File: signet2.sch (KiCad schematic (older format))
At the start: 54 parts, among them IC1 THGBMHG8C2LBAIL, J1 480372200, J3 Conn_01x02_Male, SW1 EVQ_PLDA15, U1 LDFM33PUR, U2 STM32F733IEKx, U3 USBULC6-2M6, Y1 ABM10-167-12.000MHZ-T3

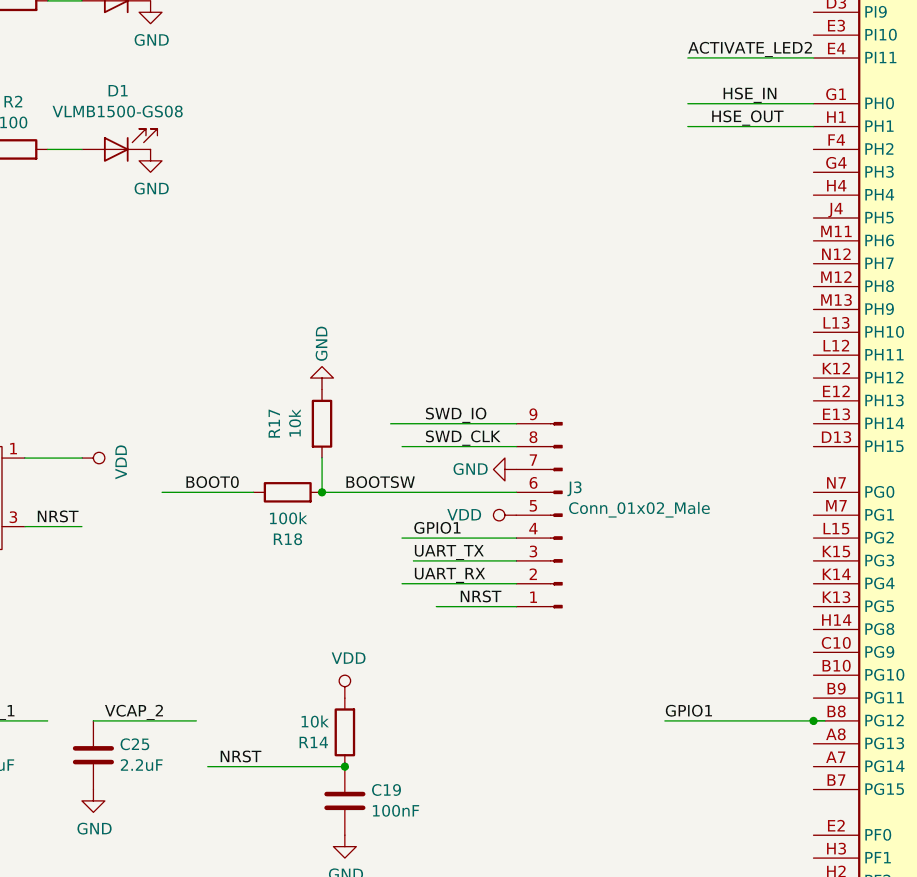
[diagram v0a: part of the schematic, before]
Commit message: Thermal and mechanical improvements
- Change user header to round through hole pads
- Remove most GND pour areas around user header GND pin so it is easier
to heat and solder/desolder
- Tighten fit of USB connector mounting slots
- Reduce the size of the increased thickness area at USB connector
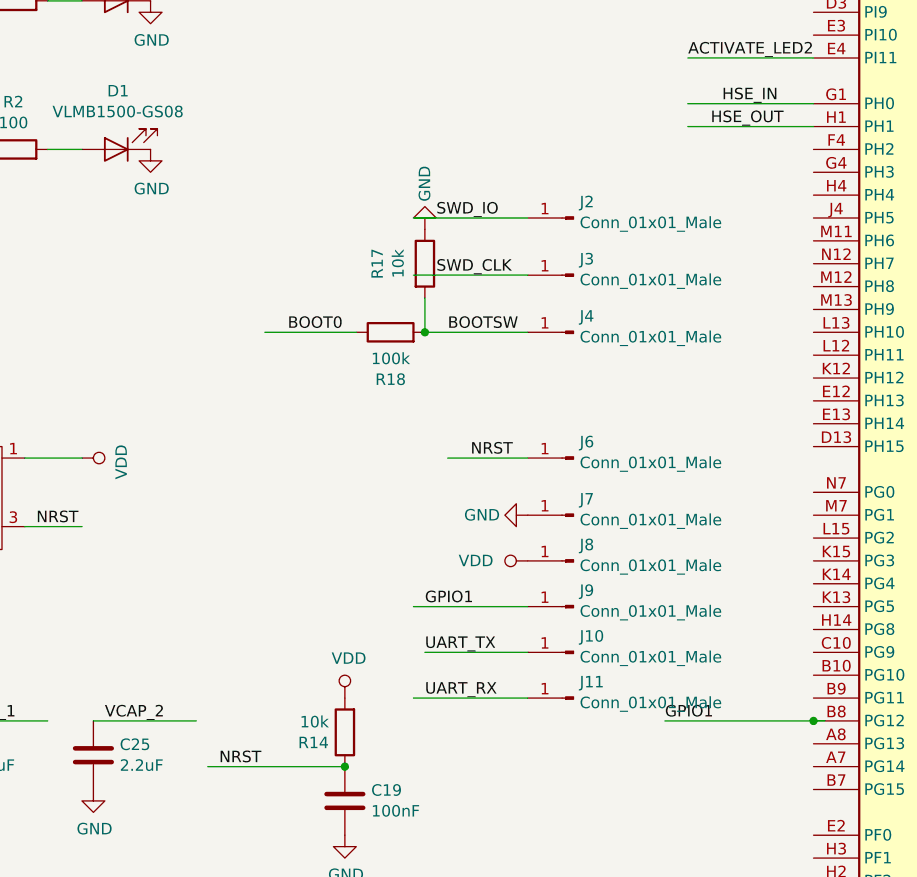
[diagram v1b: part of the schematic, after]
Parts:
- removed J3: Conn_01x02_Male, Connector_PinHeader_1.27mm:PinHeader_1x09_P1.27mm_Vertical, symbol Connector:Conn_01x09_Male
- added J10, J11, J2, J3, J4, J6, J7, J8, J9: Conn_01x01_Male, TestPoint:TestPoint_Pad_1.5x1.5mm, symbol Connector:Conn_01x01_Male
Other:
- moved on the sheet: R17, R18
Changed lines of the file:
@@
 L power:VDD #PWR0136
 U 1 1 5C81E9BA
-P 9250 6550
-F 0 "#PWR0136" H 9250 6400 50  0001 C CNN
-F 1 "VDD" V 9250 6700 50  0000 L CNN
-F 2 "" H 9250 6550 50  0001 C CNN
-F 3 "" H 9250 6550 50  0001 C CNN
-	1    9250 6550
+P 9300 6750
+F 0 "#PWR0136" H 9300 6600 50  0001 C CNN
+F 1 "VDD" V 9300 6900 50  0000 L CNN
+F 2 "" H 9300 6750 50  0001 C CNN
+F 3 "" H 9300 6750 50  0001 C CNN
+	1    9300 6750
 	0    -1   -1   0
 $EndComp
@@
 Text Label 7450 10700 0    50   ~ 0
 USB_HS_D_P
-Text Label 8500 6450 0    50   ~ 0
+Text Label 8950 5750 0    50   ~ 0
 BOOTSW
 Wire Wire Line
-	9250 6850 8750 6850
-Text Label 8800 6850 0    50   ~ 0
+	9300 7350 8800 7350
+Text Label 8850 7350 0    50   ~ 0
 UART_RX
-Text Label 8800 6750 0    50   ~ 0
+Text Label 8850 7150 0    50   ~ 0
 UART_TX
 Wire Wire Line
@@
 L Device:R R17
 U 1 1 5C85E1CB
-P 8400 6150
-F 0 "R17" V 8193 6150 50  0000 C CNN
-F 1 "10k" V 8284 6150 50  0000 C CNN
-F 2 "Resistor_SMD:R_0201_0603Metric" V 8330 6150 50  0001 C CNN
-F 3 "~" H 8400 6150 50  0001 C CNN
-	1    8400 6150
+P 8850 5450
+F 0 "R17" V 8643 5450 50  0000 C CNN
+F 1 "10k" V 8734 5450 50  0000 C CNN
+F 2 "Resistor_SMD:R_0201_0603Metric" V 8780 5450 50  0001 C CNN
+F 3 "~" H 8850 5450 50  0001 C CNN
+	1    8850 5450
 	1    0    0    -1
 $EndComp
@@
 L power:GND #PWR0151
 U 1 1 5C8CC33B
-P 9250 6350
-F 0 "#PWR0151" H 9250 6100 50  0001 C CNN
-F 1 "GND" V 9250 6150 50  0000 C CNN
-F 2 "" H 9250 6350 50  0001 C CNN
-F 3 "" H 9250 6350 50  0001 C CNN
-	1    9250 6350
+P 9300 6550
+F 0 "#PWR0151" H 9300 6300 50  0001 C CNN
+F 1 "GND" V 9300 6350 50  0000 C CNN
+F 2 "" H 9300 6550 50  0001 C CNN
+F 3 "" H 9300 6550 50  0001 C CNN
+	1    9300 6550
 	0    1    1    0
 $EndComp
-Text Label 8800 6650 0    50   ~ 0
+Text Label 8850 6950 0    50   ~ 0
 GPIO1
-Text Label 7800 6450 0    50   ~ 0
+Text Label 8250 5750 0    50   ~ 0
 BOOT0
 Wire Wire Line
-	8750 6650 9250 6650
-Wire Wire Line
-	9250 6750 8800 6750
-Wire Wire Line
-	7700 6450 8100 6450
-Wire Wire Line
-	8400 6450 9250 6450
+	8800 6950 9300 6950
+Wire Wire Line
+	9300 7150 8850 7150
+Wire Wire Line
+	8150 5750 8550 5750
 Wire Wire Line
 	7450 10700 7900 10700
@@
 	1    0    0    -1
 $EndComp
-$Comp
-L Connector:Conn_01x09_Male J3
-U 1 1 5D2ECF3B
-P 9450 6550
-F 0 "J3" H 9423 6430 50  0000 R CNN
-F 1 "Conn_01x02_Male" H 9423 6521 50  0000 R CNN
-F 2 "Connector_PinHeader_1.27mm:PinHeader_1x09_P1.27mm_Vertical" H 9450 6550 50  0001 C CNN
-F 3 "~" H 9450 6550 50  0001 C CNN
-	1    9450 6550
-	-1   0    0    1
-$EndComp
 Connection ~ 9400 1850
 Connection ~ 9400 2150
@@
 	10550 7450 9900 7450
 Wire Wire Line
-	8400 6300 8400 6450
+	8850 5600 8850 5750
 Wire Wire Line
 	15450 2450 15950 2450
@@
 SWD_CLK
 Wire Wire Line
-	8700 6150 9250 6150
-Wire Wire Line
-	8750 6250 9250 6250
-Text Label 8850 6150 0    50   ~ 0
+	8800 5250 9300 5250
+Wire Wire Line
+	8800 5500 9300 5500
+Text Label 8900 5250 0    50   ~ 0
 SWD_IO
-Text Label 8850 6250 0    50   ~ 0
+Text Label 8900 5500 0    50   ~ 0
 SWD_CLK
 $Comp
 L Device:R R18
 U 1 1 5D27F53D
-P 8250 6450
-F 0 "R18" V 8043 6450 50  0000 C CNN
-F 1 "100k" V 8134 6450 50  0000 C CNN
-F 2 "Resistor_SMD:R_0201_0603Metric" V 8180 6450 50  0001 C CNN
-F 3 "~" H 8250 6450 50  0001 C CNN
-	1    8250 6450
-	0    -1   -1   0
-$EndComp
-Connection ~ 8400 6450
+P 8700 5750
+F 0 "R18" V 8493 5750 50  0000 C CNN
+F 1 "100k" V 8584 5750 50  0000 C CNN
+F 2 "Resistor_SMD:R_0201_0603Metric" V 8630 5750 50  0001 C CNN
+F 3 "~" H 8700 5750 50  0001 C CNN
+	1    8700 5750
+	0    -1   -1   0
+$EndComp
 $Comp
 L power:GND #PWR0122
 U 1 1 5D2F4A28
-P 8400 6000
-F 0 "#PWR0122" H 8400 5750 50  0001 C CNN
-F 1 "GND" V 8400 5800 50  0000 C CNN
-F 2 "" H 8400 6000 50  0001 C CNN
-F 3 "" H 8400 6000 50  0001 C CNN
-	1    8400 6000
+P 8850 5300
+F 0 "#PWR0122" H 8850 5050 50  0001 C CNN
+F 1 "GND" V 8850 5100 50  0000 C CNN
+F 2 "" H 8850 5300 50  0001 C CNN
+F 3 "" H 8850 5300 50  0001 C CNN
+	1    8850 5300
 	-1   0    0    1
 $EndComp
@@
 EMMC_DAT7
 Wire Wire Line
-	8900 6950 9250 6950
-Text Label 9000 6950 0    50   ~ 0
+	8950 6300 9300 6300
+Text Label 9050 6300 0    50   ~ 0
 NRST
 Connection ~ 10550 7450
@@
 Wire Wire Line
 	3750 6600 3250 6600
+Wire Wire Line
+	8850 5750 9300 5750
+Connection ~ 8850 5750
+$Comp
+L Connector:Conn_01x01_Male J2
+U 1 1 5DB8B739
+P 9500 5250
+F 0 "J2" H 9473 5180 50  0000 R CNN
+F 1 "Conn_01x01_Male" H 9473 5271 50  0000 R CNN
+F 2 "TestPoint:TestPoint_Pad_1.5x1.5mm" H 9500 5250 50  0001 C CNN
+F 3 "~" H 9500 5250 50  0001 C CNN
+	1    9500 5250
+	-1   0    0    1
+$EndComp
+$Comp
+L Connector:Conn_01x01_Male J3
+U 1 1 5DB8BB45
+P 9500 5500
+F 0 "J3" H 9473 5430 50  0000 R CNN
+F 1 "Conn_01x01_Male" H 9473 5521 50  0000 R CNN
+F 2 "TestPoint:TestPoint_Pad_1.5x1.5mm" H 9500 5500 50  0001 C CNN
+F 3 "~" H 9500 5500 50  0001 C CNN
+	1    9500 5500
+	-1   0    0    1
+$EndComp
+$Comp
+L Connector:Conn_01x01_Male J6
+U 1 1 5DBDE268
+P 9500 6300
+F 0 "J6" H 9473 6230 50  0000 R CNN
+F 1 "Conn_01x01_Male" H 9473 6321 50  0000 R CNN
+F 2 "TestPoint:TestPoint_Pad_1.5x1.5mm" H 9500 6300 50  0001 C CNN
+F 3 "~" H 9500 6300 50  0001 C CNN
+	1    9500 6300
+	-1   0    0    1
+$EndComp
+$Comp
+L Connector:Conn_01x01_Male J7
+U 1 1 5DBF2C1F
+P 9500 6550
+F 0 "J7" H 9473 6480 50  0000 R CNN
+F 1 "Conn_01x01_Male" H 9473 6571 50  0000 R CNN
+F 2 "TestPoint:TestPoint_Pad_1.5x1.5mm" H 9500 6550 50  0001 C CNN
+F 3 "~" H 9500 6550 50  0001 C CNN
+	1    9500 6550
+	-1   0    0    1
+$EndComp
+$Comp
+L Connector:Conn_01x01_Male J8
+U 1 1 5DC075D7
+P 9500 6750
+F 0 "J8" H 9473 6680 50  0000 R CNN
+F 1 "Conn_01x01_Male" H 9473 6771 50  0000 R CNN
+F 2 "TestPoint:TestPoint_Pad_1.5x1.5mm" H 9500 6750 50  0001 C CNN
+F 3 "~" H 9500 6750 50  0001 C CNN
+	1    9500 6750
+	-1   0    0    1
+$EndComp
+$Comp
+L Connector:Conn_01x01_Male J9
+U 1 1 5DC1BF8E
+P 9500 6950
+F 0 "J9" H 9473 6880 50  0000 R CNN
+F 1 "Conn_01x01_Male" H 9473 6971 50  0000 R CNN
+F 2 "TestPoint:TestPoint_Pad_1.5x1.5mm" H 9500 6950 50  0001 C CNN
+F 3 "~" H 9500 6950 50  0001 C CNN
+	1    9500 6950
+	-1   0    0    1
+$EndComp
+$Comp
+L Connector:Conn_01x01_Male J10
+U 1 1 5DC30952
+P 9500 7150
+F 0 "J10" H 9473 7080 50  0000 R CNN
+F 1 "Conn_01x01_Male" H 9473 7171 50  0000 R CNN
+F 2 "TestPoint:TestPoint_Pad_1.5x1.5mm" H 9500 7150 50  0001 C CNN
+F 3 "~" H 9500 7150 50  0001 C CNN
+	1    9500 7150
+	-1   0    0    1
+$EndComp
+$Comp
+L Connector:Conn_01x01_Male J11
+U 1 1 5DC45313
+P 9500 7350
+F 0 "J11" H 9473 7280 50  0000 R CNN
+F 1 "Conn_01x01_Male" H 9473 7371 50  0000 R CNN
+F 2 "TestPoint:TestPoint_Pad_1.5x1.5mm" H 9500 7350 50  0001 C CNN
+F 3 "~" H 9500 7350 50  0001 C CNN
+	1    9500 7350
+	-1   0    0    1
+$EndComp
+$Comp
+L Connector:Conn_01x01_Male J4
+U 1 1 5DBA0501
+P 9500 5750
+F 0 "J4" H 9473 5680 50  0000 R CNN
+F 1 "Conn_01x01_Male" H 9473 5771 50  0000 R CNN
+F 2 "TestPoint:TestPoint_Pad_1.5x1.5mm" H 9500 5750 50  0001 C CNN
+F 3 "~" H 9500 5750 50  0001 C CNN
+	1    9500 5750
+	-1   0    0    1
+$EndComp
 $EndSCHEMATC

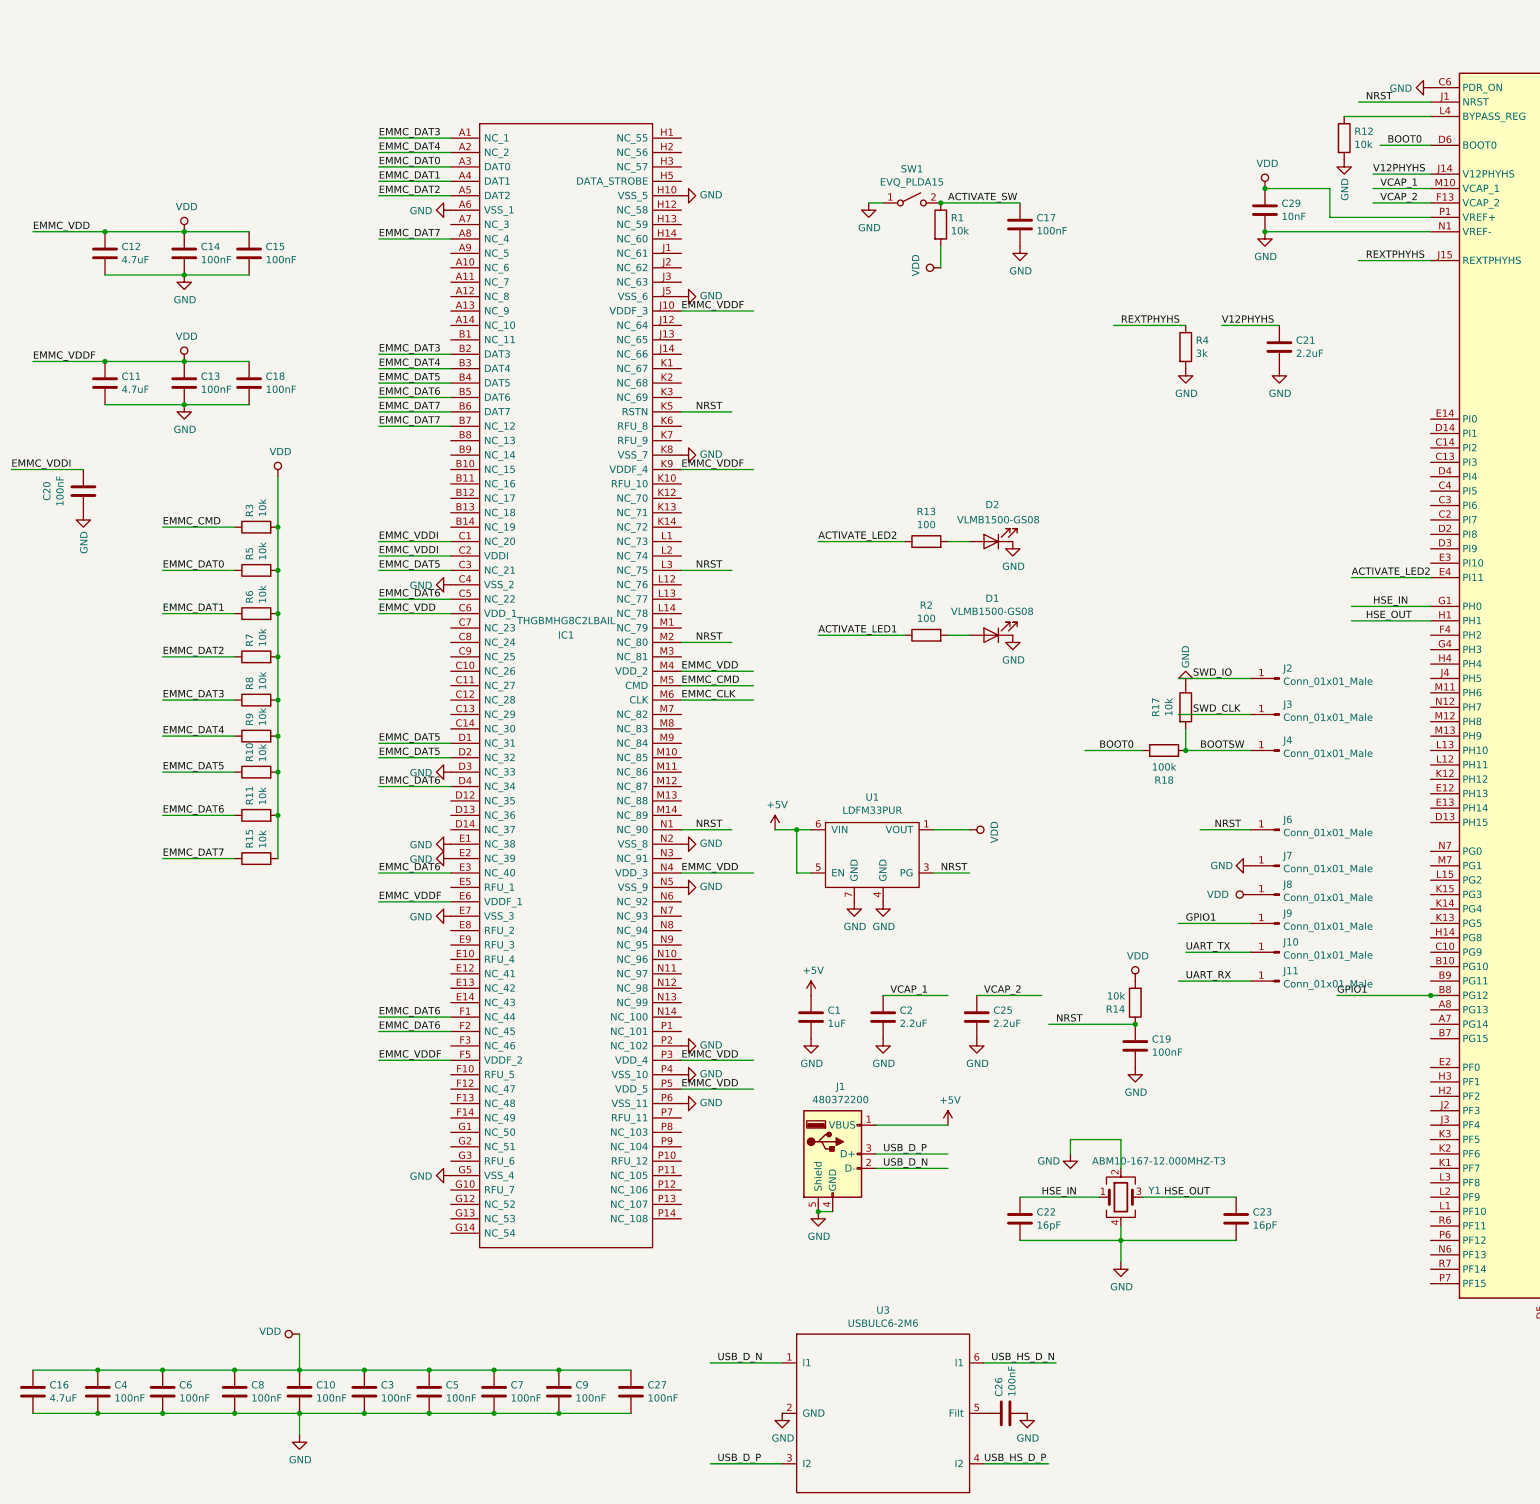
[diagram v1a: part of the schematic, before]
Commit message: Version 1.22
- Add GND plane pour to GND line through-hole connection
- Change visual layout in schematic (connections are the same)
- Make area sticking out near USB port smaller. Needed to take into
consideration the possible need for the port to be able to bend
slightly down to fit in enclosure. This will depend on the exact PCB
thickness and how the USB port seats on it.
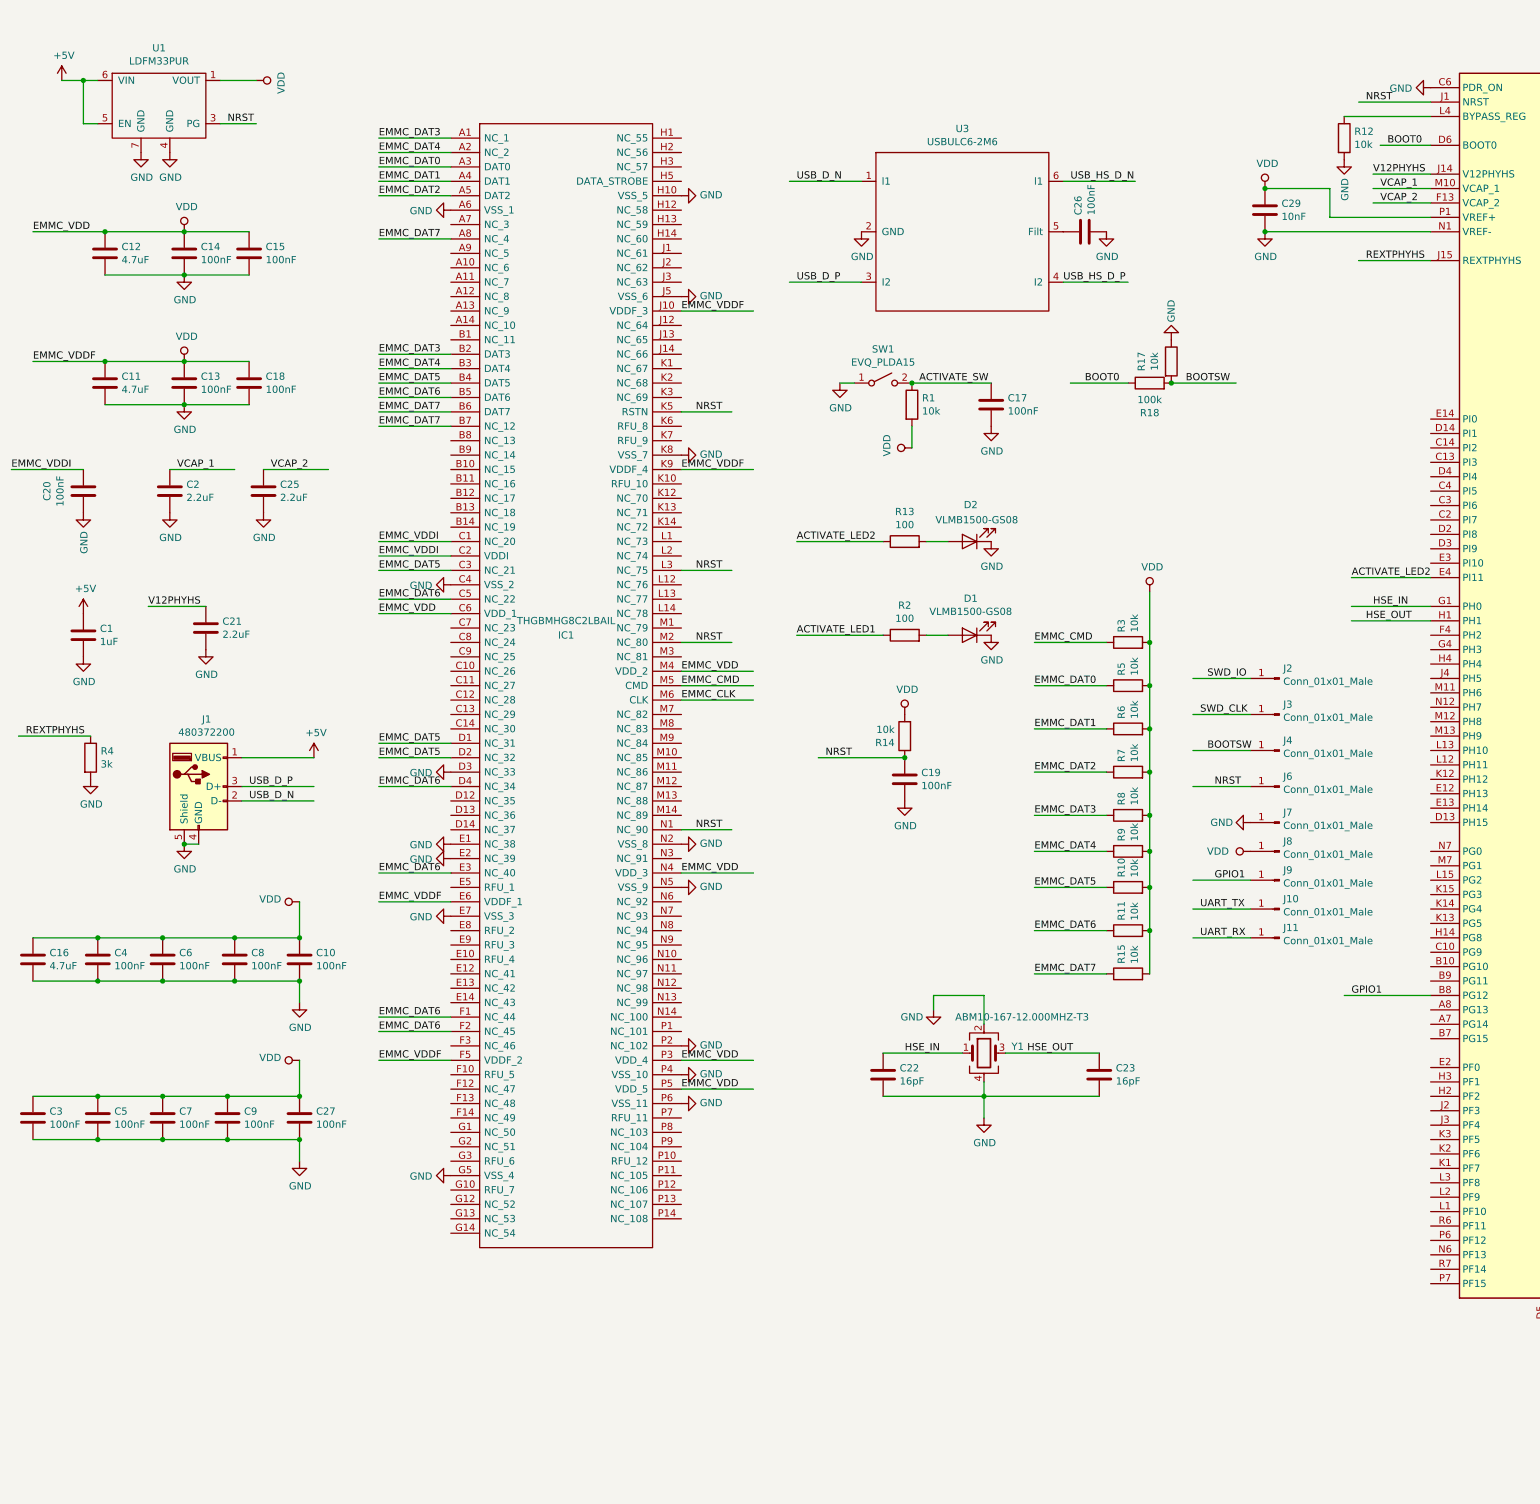
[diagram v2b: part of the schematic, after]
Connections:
- wire segments 219 -> 218
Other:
- moved on the sheet: C1, C10, C16, C17, C19, C2, C21, C22, C23, C25, C26, C27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
